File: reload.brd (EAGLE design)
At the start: 50 x 31 mm, 25 parts, among them IC1 OPAMP-DUALMS, IC2 V_REG_MIC2920, Q1 BTS117, Q2 BTS117

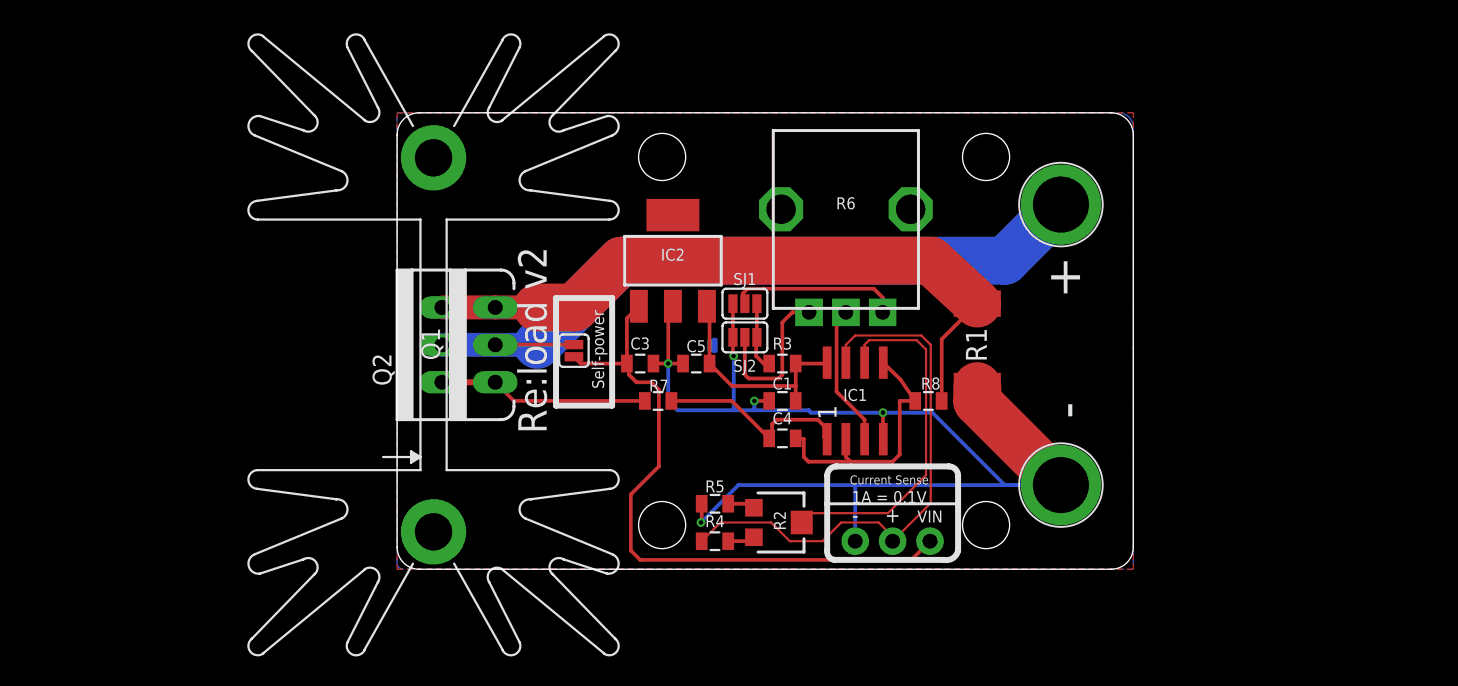
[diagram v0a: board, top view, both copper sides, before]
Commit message: change components and layout
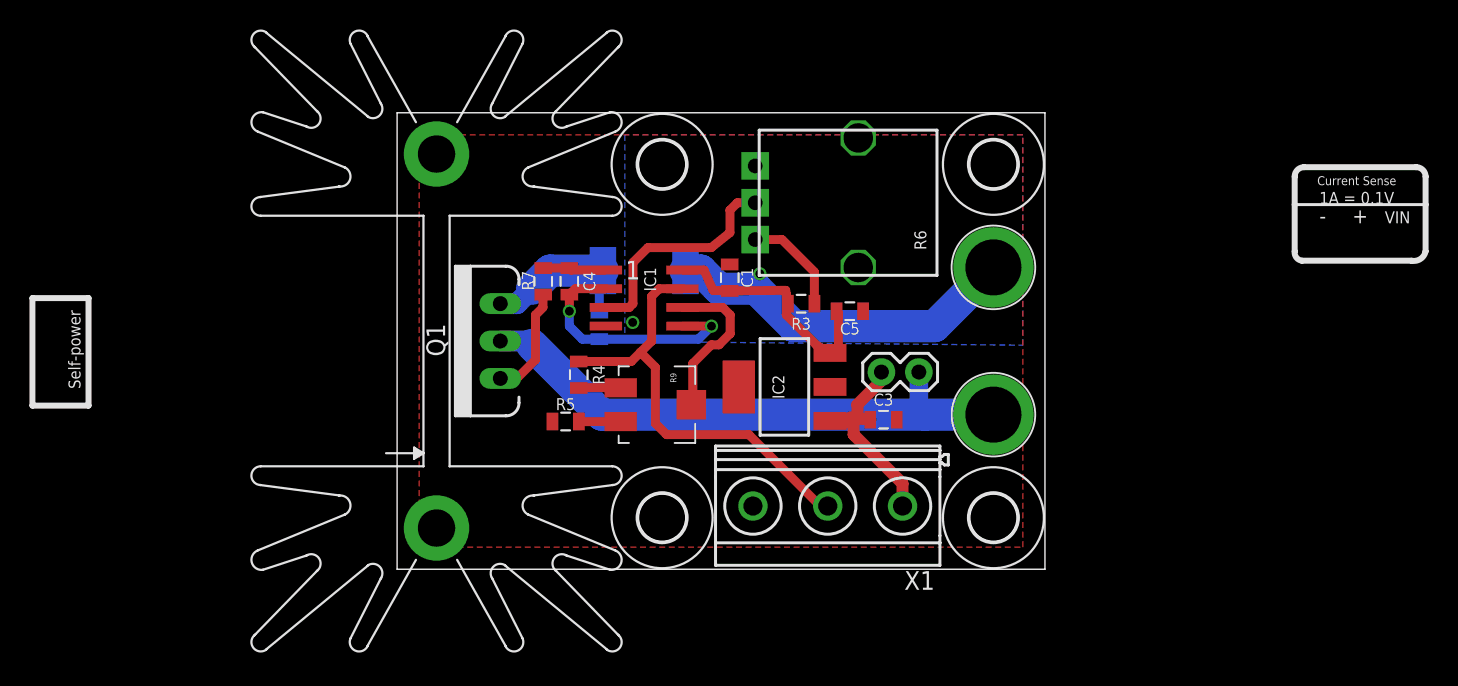
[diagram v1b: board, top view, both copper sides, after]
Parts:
- removed JP1: (no value), SparkFun-Connectors:1X03_NO_SILK
- removed Q2: BTS117, SparkFun-DiscreteSemi:TO220V
- removed R2: 1k, nickparts:TRIMPOT-3MM-2
- removed SJ1: (no value), SparkFun-Passives:SJ_3_PASTE2&3
- removed SJ2: (no value), SparkFun-Passives:SJ_3_PASTE1&2
- added R9: 10k, trimmer:TRIMPOT-5MM
- added U$1, U$4: (no value), holes:3,2
- added X1: MKDSN1,5/3-5,08, con-phoenix-508:MKDSN1,5/3-5,08
- IC1: value OPAMP-DUALMS -> MCP6002
- IC2: value V_REG_MIC2920 -> TS 1117
- JP2: device SparkFun-Passives:SJ_2S -> SparkFun-Passives:1X02
- Q1: value BTS117 -> IRLZ34N
- R1: value 0.05 1% -> 0.1 1%
- R3: value 162k -> 100k
- R4: value 10k 1% -> 100k 1%
- U$2: device nickparts:ARACHNID_LABS_LOGO_SM -> holes:3,2
- U$3: device SparkFun-Aesthetics:OSHW-LOGO-M -> holes:3,2
- moved R1 23.2 mm to (16.8, 20.3), flipped to the bottom, turned to 0 degrees
- moved U$2 23.0 mm to (40.5, 3.50), flipped to the top, turned to 0 degrees
- moved R8 22.9 mm to (13.7, 16.5), flipped to the bottom, turned to 270 degrees
- moved JP2 20.9 mm to (32.9, 13.4), turned to 0 degrees
- moved C4 18.0 mm to (11.7, 19.6), turned to 270 degrees
- moved C3 17.0 mm to (33.0, 10.2)
- moved IC1 15.9 mm to (16.8, 18.4), turned to 270 degrees
- moved J2 15.5 mm to (40.5, 20.5)
- moved J1 15.0 mm to (40.5, 10.5)
- moved R4 14.6 mm to (12.3, 13.2), turned to 270 degrees
- moved U$3 13.2 mm to (18.0, 3.50), flipped to the top, turned to 0 degrees
- moved R5 11.6 mm to (11.4, 10.0)
- moved IC2 11.4 mm to (26.3, 12.4), turned to 90 degrees
- moved R7 11.3 mm to (9.92, 19.6), turned to 90 degrees
- moved C5 11.0 mm to (30.8, 17.5), turned to 0 degrees
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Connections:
- removed net N$10: R3.1, SJ1.3, SJ2.3
- removed net N$8: R6.P$1, SJ2.2
- net GND: now also R6.P$1, X1.3; no longer JP1.1, SJ1.1, SJ2.1
- net IREF: now also X1.2; no longer JP1.2
- net N$2: now also R3.1; no longer SJ1.2
- net N$3: no longer Q2.3
- net N$5: now also R9.B; no longer R2.2
- net N$6: now also R9.A; no longer R2.1
- net N$7: now also R9.C; no longer R2.3
- net N$9: no longer Q2.1
- net V+: no longer Q2.2
- net VDD: now also X1.1; no longer JP1.3
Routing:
- net GND: track 89.2 -> 24.1 mm, vias 5 -> 2
- net N$3: track 46.4 -> 10.8 mm
- net VDD: track 44.2 -> 14.3 mm
- net N$5: track 24.3 -> 10.9 mm
- net V+: track 51.8 -> 38.7 mm
- net N$8: track 10.9 -> 0.00 mm
- net N$1: track 13.7 -> 4.31 mm
- net IREF: track 37.2 -> 30.2 mm
- net N$9: track 14.3 -> 7.55 mm
- net N$4: track 9.67 -> 15.6 mm
- net N$10: track 4.70 -> 0.00 mm
- net N$2: track 11.7 -> 7.09 mm
- net VCC: track 15.5 -> 18.3 mm
- net SENSE: track 18.4 -> 17.1 mm, vias 0 -> 2
- net N$6: track 2.32 -> 2.84 mm
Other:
- board size 50 x 31 mm -> 44 x 31 mm
- board text removed: "Re:load v2"
- board text removed: "github.com/arachnidlabs/reload"

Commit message: change board layout
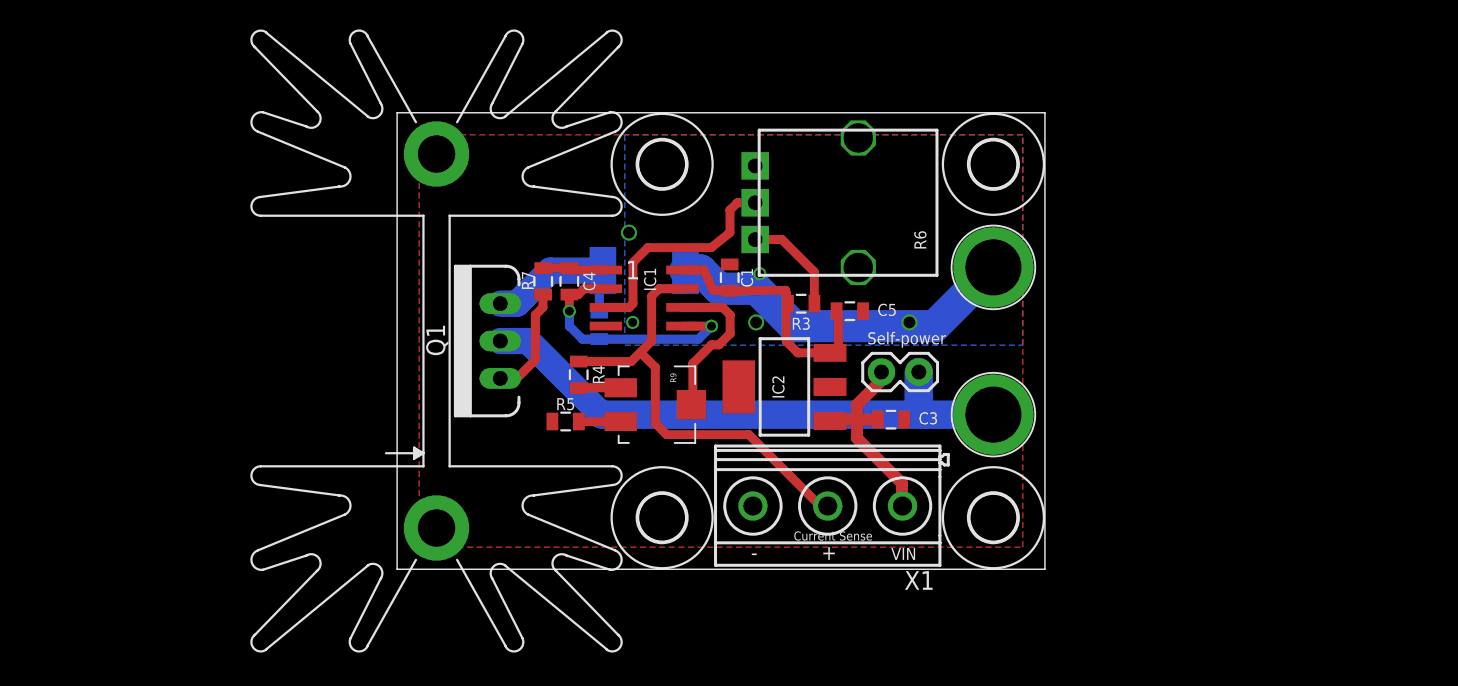
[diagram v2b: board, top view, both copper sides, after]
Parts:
- moved C3 0.51 mm to (33.5, 10.2)
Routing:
- net VCC: track 18.3 -> 19.4 mm
- net GND: vias 2 -> 5
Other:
- board text removed: "1A = 0.1V"
